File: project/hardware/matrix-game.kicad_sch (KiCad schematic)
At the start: 28 parts, among them SW1 button_center, SW2 button_left, SW3 button_down, SW4 button_right, SW5 button_up, U1 NUCLEO-F042K6, U2 MAX7219, U3 SSD1306

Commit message: [project/hardware] added jumper for buzzer
Signed-off-by: Timon Burkard <timon.burkard@gwf.ch>
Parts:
- added JP1: Jumper_2_Bridged, Connector_PinHeader_2.54mm:PinHeader_1x02_P2.54mm_Vertical, symbol Jumper:Jumper_2_Bridged
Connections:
- net at U1.CN4_9 (PA4/A3): now also JP1.1 (A); no longer BZ1.1 (+)
- new net: BZ1.1 (+), JP1.2 (B)
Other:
- moved on the sheet: BZ1
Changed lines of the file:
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@@
 	(wire
 		(pts
-			(xy 179.07 101.6) (xy 179.07 105.41)
-		)
-		(stroke
-			(width 0)
-			(type default)
-		)
-	)
-	(wire
-		(pts
 			(xy 213.36 31.75) (xy 213.36 43.18)
 		)
@@
 	(wire
 		(pts
+			(xy 193.04 101.6) (xy 193.04 105.41)
+		)
+		(stroke
+			(width 0)
+			(type default)
+		)
+	)
+	(wire
+		(pts
 			(xy 261.62 40.64) (xy 275.59 40.64)
 		)
@@
 	(wire
 		(pts
+			(xy 187.96 96.52) (xy 193.04 96.52)
+		)
+		(stroke
+			(width 0)
+			(type default)
+		)
+	)
+	(wire
+		(pts
 			(xy 228.6 53.34) (xy 231.14 53.34)
 		)
@@
 	(wire
 		(pts
-			(xy 149.86 96.52) (xy 179.07 96.52)
+			(xy 149.86 96.52) (xy 177.8 96.52)
 		)
 		(stroke
@@
 	(symbol
 		(lib_id "power:GND")
-		(at 179.07 105.41 0)
+		(at 193.04 105.41 0)
 		(unit 1)
 		(exclude_from_sim no)
@@
 		(fields_autoplaced yes)
 		(property "Reference" "#PWR09"
-			(at 179.07 111.76 0)
+			(at 193.04 111.76 0)
 			(effects
 				(font
@@
 		)
 		(property "Value" "GND"
-			(at 179.07 110.49 0)
+			(at 193.04 110.49 0)
 			(effects
 				(font
@@
 		)
 		(property "Footprint" ""
-			(at 179.07 105.41 0)
+			(at 193.04 105.41 0)
 			(effects
 				(font
@@
 		)
 		(property "Datasheet" ""
-			(at 179.07 105.41 0)
+			(at 193.04 105.41 0)
 			(effects
 				(font
@@
 		)
 		(property "Description" "Power symbol creates a global label with name \"GND\" , ground"
-			(at 179.07 105.41 0)
+			(at 193.04 105.41 0)
 			(effects
 				(font
@@
 	(symbol
 		(lib_id "Device:Buzzer")
-		(at 181.61 99.06 0)
+		(at 195.58 99.06 0)
 		(unit 1)
 		(exclude_from_sim no)
@@
 		(fields_autoplaced yes)
 		(property "Reference" "BZ1"
-			(at 185.42 97.7899 0)
+			(at 199.39 97.7899 0)
 			(effects
 				(font
@@
 		)
 		(property "Value" "buzzer"
-			(at 185.42 100.3299 0)
+			(at 199.39 100.3299 0)
 			(effects
 				(font
@@
 		)
 		(property "Footprint" "Buzzer_Beeper:Buzzer_12x9.5RM7.6"
-			(at 180.975 96.52 90)
+			(at 194.945 96.52 90)
 			(effects
 				(font
@@
 		)
 		(property "Datasheet" "~"
-			(at 180.975 96.52 90)
+			(at 194.945 96.52 90)
 			(effects
 				(font
@@
 		)
 		(property "Description" "Buzzer, polarized"
-			(at 181.61 99.06 0)
+			(at 195.58 99.06 0)
 			(effects
 				(font
@@
 					(unit 1)
 				)
+			)
+		)
+	)
+	(symbol
+		(lib_id "Jumper:Jumper_2_Bridged")
+		(at 182.88 96.52 0)
+		(unit 1)
+		(exclude_from_sim yes)
+		(in_bom yes)
+		(on_board yes)
+		(dnp no)
+		(fields_autoplaced yes)
+		(property "Reference" "JP1"
+			(at 182.88 91.44 0)
+			(effects
+				(font
+					(size 1.27 1.27)
+				)
+			)
+		)
+		(property "Value" "Jumper_2_Bridged"
+			(at 182.88 93.98 0)
+			(effects
+				(font
+					(size 1.27 1.27)
+				)
+			)
+		)
+		(property "Footprint" "Connector_PinHeader_2.54mm:PinHeader_1x02_P2.54mm_Vertical"
+			(at 182.88 96.52 0)
+			(effects
+				(font
+					(size 1.27 1.27)
+				)
+				(hide yes)
+			)
+		)
+		(property "Datasheet" "~"
+			(at 182.88 96.52 0)
+			(effects
+				(font
+					(size 1.27 1.27)
+				)
+				(hide yes)
+			)
+		)
+		(property "Description" "Jumper, 2-pole, closed/bridged"
+			(at 182.88 96.52 0)
+			(effects
+				(font
+					(size 1.27 1.27)
+				)
+				(hide yes)
+			)
+		)
+		(pin "1"
+		)
+		(pin "2"
+		)
+		(instances
+			(project ""
+				(path "/84955768-42fa-4149-b8df-35c5d6dc27b9"
+					(reference "JP1")
+					(unit 1)
+				)

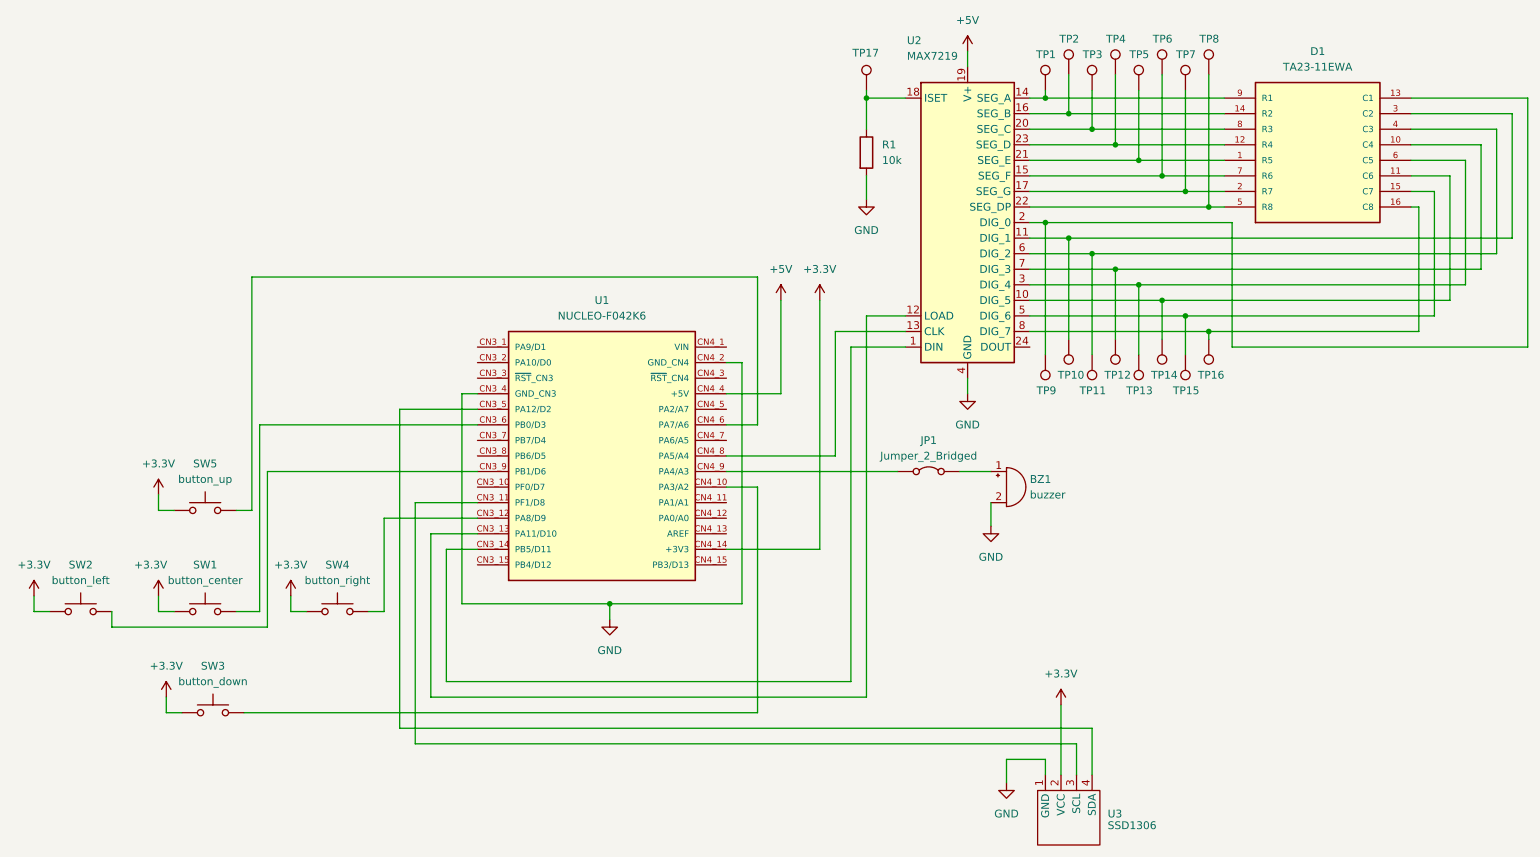
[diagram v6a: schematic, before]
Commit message: [project/hardware] added capacitors for LCD and MAX7219, logo and version
Signed-off-by: Timon Burkard <timon.burkard@gwf.ch>
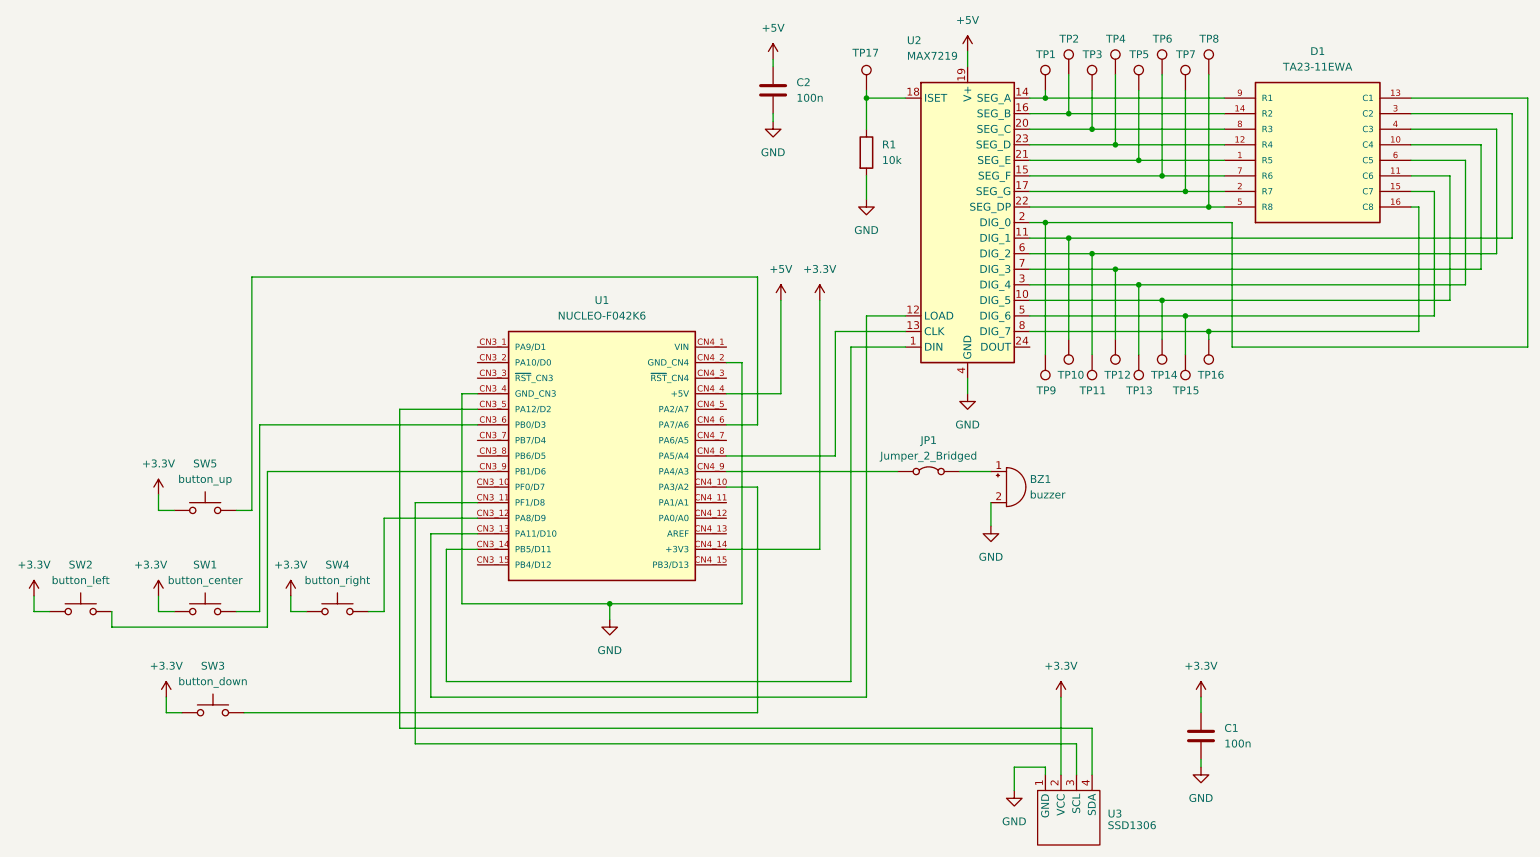
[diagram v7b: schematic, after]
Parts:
- added C1, C2: 100n, Capacitor_THT:C_Disc_D3.0mm_W2.0mm_P2.50mm, symbol Device:C
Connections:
- net +3.3V: now also C1.1
- net +5V: now also C2.1
- net GND: now also C1.2, C2.2

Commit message: [project/hardware] added page settings
Signed-off-by: Timon Burkard <timon.burkard@gwf.ch>
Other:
- company: (none) -> GWF AG
- title: (none) -> Schnupperlehre Elektroniker/in | Projekt Matrix-Game
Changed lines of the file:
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@@
 	(generator_version "8.0")
 	(paper "A4")
+	(title_block
+		(title "Schnupperlehre Elektroniker/in | Projekt Matrix-Game")
+		(date "2025-02-07")
+		(rev "v1.0")
+		(company "GWF AG")
+		(comment 1 "Timon Burkard")
+	)
 	(junction
 		(at 205.74 58.42)
